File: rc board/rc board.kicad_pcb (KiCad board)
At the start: 2 copper layers, 95 parts, among them J1 Bypass, J10 3S, J11 4S, J12 5S, J13 6S, J14 Mot_0, J15 Mot_1, J16 Mot_3, J17 Mot_2, J2 Bypass, J3 Bypass, J4 Throttle_in, J5 Throttle_out, J6 CH3_in, J7 CH3_out, J8 Steering_in, J9 Steering_out, U1 DRV10983, U2 DRV10983, U3 DRV10983, U4 DRV10983

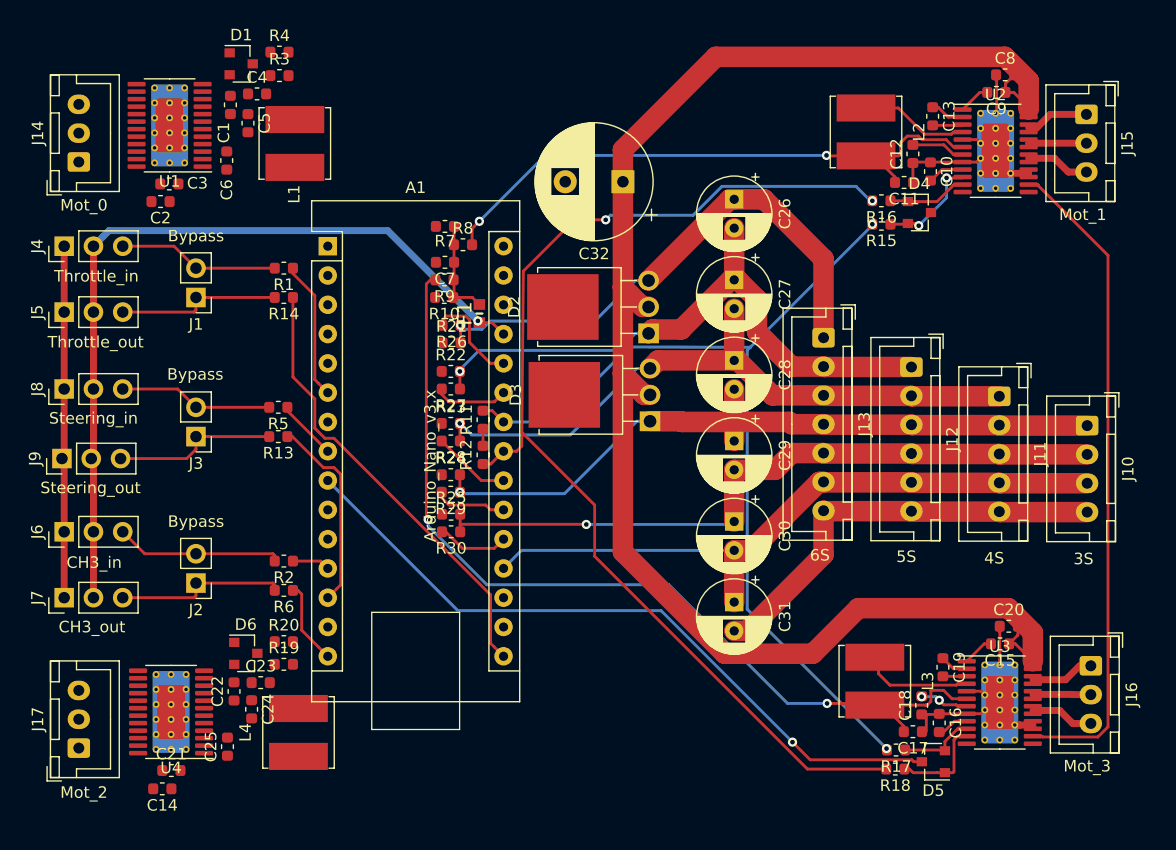
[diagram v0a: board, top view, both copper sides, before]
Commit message: Finished routing all the signals, except for some GNDs that probably need filling.
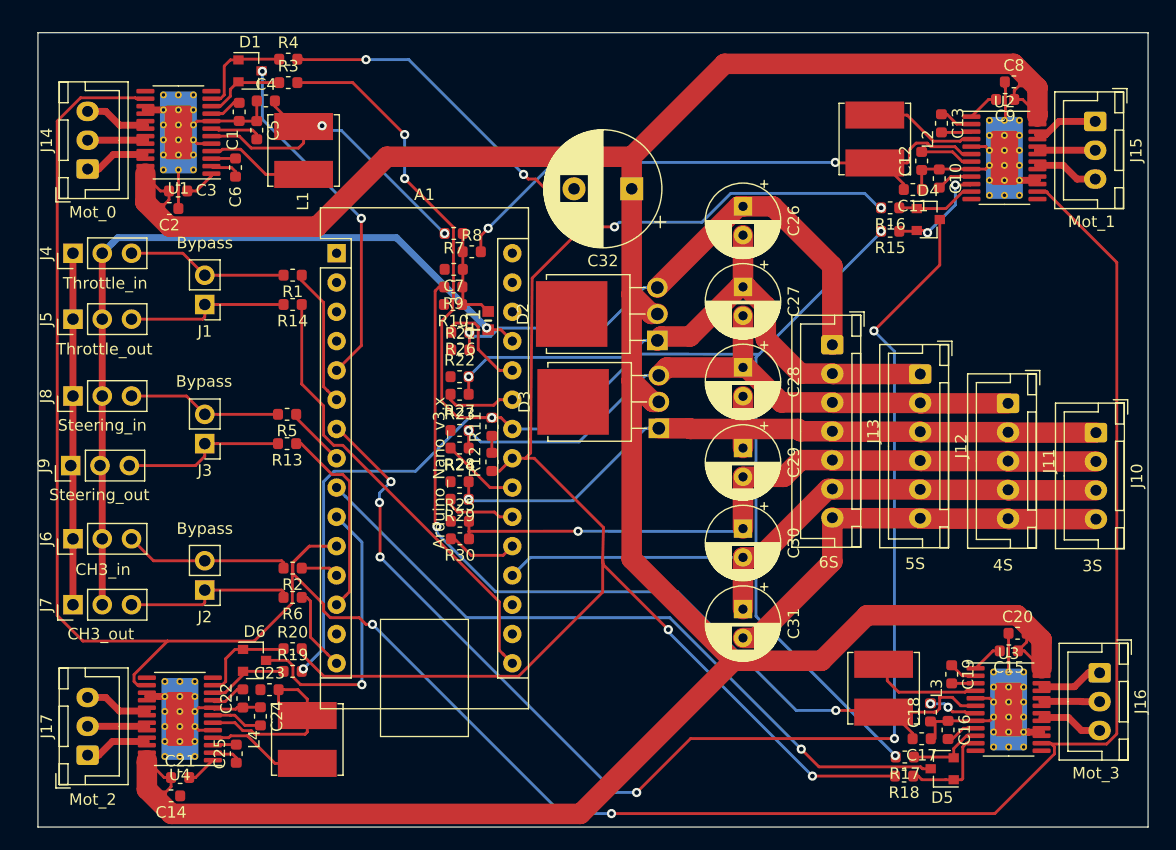
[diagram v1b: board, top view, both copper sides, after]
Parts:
- moved A1 0.98 mm to (40.3, 34.3)
- moved C1 0.98 mm to (31.9, 22.0)
- moved C10 0.98 mm to (92.6, 27.8)
- moved C11 0.98 mm to (90.3, 28.7)
- moved C12 0.98 mm to (91.1, 26.3)
- moved C13 0.98 mm to (92.8, 23.0)
- moved C14 0.98 mm to (26.0, 81.3)
- moved C15 0.98 mm to (98.6, 68.7)
- moved C16 0.98 mm to (93.3, 75.6)
- moved C17 0.98 mm to (91.1, 76.4)
- moved C18 0.98 mm to (91.8, 74.1)
- moved C19 0.98 mm to (93.7, 70.8)
- moved C2 0.98 mm to (25.8, 30.4)
- moved C20 0.98 mm to (99.4, 67.2)
- moved C21 0.98 mm to (26.8, 79.7)
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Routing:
- net DIR: track 57.3 -> 226.3 mm, vias 0 -> 2
- net +BATT: track 137.9 -> 256.3 mm
- net EN_1: track 0.00 -> 116.7 mm, vias 0 -> 6
- net SCL: track 81.4 -> 156.9 mm, vias 2 -> 6
- net SDA: track 99.3 -> 162.6 mm, vias 2 -> 6
- net EN_0: track 0.00 -> 30.5 mm, vias 0 -> 2
- net +5V_0: track 0.00 -> 29.8 mm, vias 0 -> 2
- net EN_3: track 0.00 -> 25.2 mm, vias 0 -> 1
- net GND: track 96.8 -> 121.3 mm
- net +5V_3: track 0.00 -> 15.6 mm
- net Net-(L4-Pad1): track 0.00 -> 9.25 mm
- net Net-(L1-Pad1): track 0.00 -> 8.97 mm
- net Net-(D1-Pad1): track 0.00 -> 8.76 mm
- net Net-(D6-Pad1): track 0.00 -> 8.60 mm
- net Net-(D1-Pad2): track 0.00 -> 7.13 mm
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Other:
- board outline added: 96.3 x 68.9 mm

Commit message: 0 unconnected items!
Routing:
- net +5V_3: track 15.6 -> 60.9 mm, vias 0 -> 6
- net GND: track 121.3 -> 164.2 mm, vias 0 -> 3
- net +3V3: track 1.47 -> 20.3 mm, vias 0 -> 4
- added copper zone on B.Cu, net GND
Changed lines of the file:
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@@
     (thickness 1.6)
     (drawings 4)
-    (tracks 774)
+    (tracks 842)
     (zones 0)
     (modules 95)
@@
   (gr_line (start 110.6932 84.0232) (end 110.6932 15.1384) (layer Edge.Cuts) (width 0.05))
   (gr_line (start 14.4272 15.1384) (end 14.4272 84.0232) (layer Edge.Cuts) (width 0.05))
+  (via (at 50.2412 42.6212) (size 0.8) (drill 0.4) (layers F.Cu B.Cu) (net 16))
+  (via (at 49.6316 35.7124) (size 0.8) (drill 0.4) (layers F.Cu B.Cu) (net 16))
   (segment (start 54.762501 69.024601) (end 55.5625 69.8246) (width 0.25) (layer F.Cu) (net 1))
   (segment (start 54.437499 64.494597) (end 54.437499 68.699599) (width 0.25) (layer F.Cu) (net 1))
@@
   (segment (start 26.6065 27.461364) (end 26.60599 27.461874) (width 0.25) (layer F.Cu) (net 16))
   (segment (start 26.6065 27.0371) (end 26.6065 27.461364) (width 0.25) (layer F.Cu) (net 16))
+  (segment (start 26.6065 20.5371) (end 26.6065 17.8943) (width 3) (layer B.Cu) (net 16))
+  (segment (start 26.6065 27.0371) (end 26.6065 28.6893) (width 3) (layer B.Cu) (net 16))
+  (segment (start 98.234501 22.743601) (end 98.234501 19.469099) (width 3) (layer B.Cu) (net 16))
+  (segment (start 98.234501 29.667865) (end 98.2472 29.680564) (width 3) (layer B.Cu) (net 16))
+  (segment (start 98.234501 29.243601) (end 98.234501 29.667865) (width 3) (layer B.Cu) (net 16))
+  (segment (start 98.2472 29.680564) (end 98.2472 32.9692) (width 3) (layer B.Cu) (net 16))
+  (segment (start 98.596 70.156836) (end 98.6028 70.150036) (width 3) (layer B.Cu) (net 16))
+  (segment (start 98.596 70.5811) (end 98.596 70.156836) (width 3) (layer B.Cu) (net 16))
+  (segment (start 98.6028 70.150036) (end 98.6028 65.532) (width 3) (layer B.Cu) (net 16))
+  (segment (start 98.596 77.505364) (end 98.6028 77.512164) (width 3) (layer B.Cu) (net 16))
+  (segment (start 98.596 77.0811) (end 98.596 77.505364) (width 3) (layer B.Cu) (net 16))
+  (segment (start 98.6028 77.512164) (end 98.6028 80.01) (width 3) (layer B.Cu) (net 16))
+  (segment (start 26.7335 71.4006) (end 26.7335 68.2879) (width 3) (layer B.Cu) (net 16))
+  (segment (start 26.7335 78.324864) (end 26.7208 78.337564) (width 3) (layer B.Cu) (net 16))
+  (segment (start 26.7335 77.9006) (end 26.7335 78.324864) (width 3) (layer B.Cu) (net 16))
+  (segment (start 26.7208 78.337564) (end 26.7208 80.7212) (width 3) (layer B.Cu) (net 16))
+  (segment (start 26.759 77.9261) (end 26.7335 77.9006) (width 0.25) (layer F.Cu) (net 16))
+  (segment (start 26.759 81.3181) (end 26.759 77.9261) (width 0.25) (layer F.Cu) (net 16))
+  (segment (start 33.7185 73.6346) (end 33.7185 72.1106) (width 0.25) (layer F.Cu) (net 16))
+  (segment (start 49.44049 53.75159) (end 49.7655 54.0766) (width 0.25) (layer F.Cu) (net 16))
+  (segment (start 49.44049 49.95661) (end 49.44049 53.75159) (width 0.25) (layer F.Cu) (net 16))
+  (segment (start 49.7655 49.6316) (end 49.44049 49.95661) (width 0.25) (layer F.Cu) (net 16))
+  (segment (start 50.203 49.6316) (end 49.7655 49.6316) (width 0.25) (layer F.Cu) (net 16))
+  (segment (start 49.791 57.5056) (end 50.2285 57.5056) (width 0.25) (layer F.Cu) (net 16))
+  (segment (start 49.44049 57.15509) (end 49.791 57.5056) (width 0.25) (layer F.Cu) (net 16))
+  (segment (start 49.44049 54.40161) (end 49.44049 57.15509) (width 0.25) (layer F.Cu) (net 16))
+  (segment (start 49.7655 54.0766) (end 49.44049 54.40161) (width 0.25) (layer F.Cu) (net 16))
+  (segment (start 50.203 54.0766) (end 49.7655 54.0766) (width 0.25) (layer F.Cu) (net 16))
+  (segment (start 50.203 49.5934) (end 49.784 49.1744) (width 0.25) (layer F.Cu) (net 16))
+  (via (at 49.784 49.1744) (size 0.8) (drill 0.4) (layers F.Cu B.Cu) (net 16))
+  (segment (start 50.203 49.6316) (end 50.203 49.5934) (width 0.25) (layer F.Cu) (net 16))
+  (segment (start 50.203 42.6594) (end 50.2412 42.6212) (width 0.25) (layer F.Cu) (net 16))
+  (segment (start 50.203 44.9707) (end 50.203 42.6594) (width 0.25) (layer F.Cu) (net 16))
   (segment (start 53.7845 50.1016) (end 53.7845 51.5746) (width 0.25) (layer F.Cu) (net 17))
+  (via (at 57.4548 59.436) (size 0.8) (drill 0.4) (layers F.Cu B.Cu) (net 17))
+  (segment (start 57.4548 65.3923) (end 57.4548 59.436) (width 0.25) (layer F.Cu) (net 17))
+  (segment (start 55.5625 67.2846) (end 57.4548 65.3923) (width 0.25) (layer F.Cu) (net 17))
+  (via (at 57.4548 56.4526) (size 0.8) (drill 0.4) (layers F.Cu B.Cu) (net 17))
+  (segment (start 57.4548 59.436) (end 57.4548 56.4526) (width 0.25) (layer B.Cu) (net 17))
+  (via (at 57.4548 54.1528) (size 0.8) (drill 0.4) (layers F.Cu B.Cu) (net 17))
+  (segment (start 57.4548 56.4526) (end 57.4548 54.1528) (width 0.25) (layer F.Cu) (net 17))
+  (segment (start 56.471601 53.169601) (end 55.022499 53.169601) (width 0.25) (layer B.Cu) (net 17))
+  (segment (start 55.022499 53.169601) (end 53.848 51.995102) (width 0.25) (layer B.Cu) (net 17))
+  (segment (start 57.4548 54.1528) (end 56.471601 53.169601) (width 0.25) (layer B.Cu) (net 17))
+  (via (at 53.7845 51.5746) (size 0.8) (drill 0.4) (layers F.Cu B.Cu) (net 17))
+  (segment (start 53.848 51.6381) (end 53.7845 51.5746) (width 0.25) (layer B.Cu) (net 17))
+  (segment (start 53.848 51.995102) (end 53.848 51.6381) (width 0.25) (layer B.Cu) (net 17))
   (segment (start 54.5845 48.5266) (end 55.5625 49.5046) (width 0.25) (layer F.Cu) (net 18))
   (segment (start 53.7845 48.5266) (end 54.5845 48.5266) (width 0.25) (layer F.Cu) (net 18))
@@
   (segment (start 32.925486 75.66058) (end 33.237016 75.97211) (width 0.25) (layer F.Cu) (net 29))
   (segment (start 29.596 74.9756) (end 31.50439 74.9756) (width 0.25) (layer F.Cu) (net 29))
+  (segment (start 37.7825 74.3536) (end 40.9116 74.3536) (width 0.25) (layer F.Cu) (net 29))
+  (via (at 41.7576 72.399601) (size 0.8) (drill 0.4) (layers F.Cu B.Cu) (net 29))
+  (segment (start 38.311499 72.399601) (end 41.7576 72.399601) (width 0.25) (layer F.Cu) (net 29))
+  (segment (start 37.7825 72.9286) (end 38.311499 72.399601) (width 0.25) (layer F.Cu) (net 29))
+  (via (at 41.7946 64.3636) (size 0.8) (drill 0.4) (layers F.Cu B.Cu) (net 29))
+  (segment (start 41.7576 64.4006) (end 41.7946 64.3636) (width 0.25) (layer B.Cu) (net 29))
+  (segment (start 41.7576 72.399601) (end 41.7576 64.4006) (width 0.25) (layer B.Cu) (net 29))
+  (segment (start 41.7946 64.3636) (end 45.5168 60.6414) (width 0.25) (layer F.Cu) (net 29))
+  (via (at 45.385798 56.468202) (size 0.8) (drill 0.4) (layers F.Cu B.Cu) (net 29))
+  (segment (start 45.5168 56.599204) (end 45.385798 56.468202) (width 0.25) (layer F.Cu) (net 29))
+  (segment (start 45.5168 60.6414) (end 45.5168 56.599204) (width 0.25) (layer F.Cu) (net 29))
+  (via (at 46.02377 53.894601) (size 0.8) (drill 0.4) (layers F.Cu B.Cu) (net 29))
+  (segment (start 46.02377 55.83023) (end 46.02377 53.894601) (width 0.25) (layer B.Cu) (net 29))
+  (segment (start 45.385798 56.468202) (end 46.02377 55.83023) (width 0.25) (layer B.Cu) (net 29))
+  (via (at 48.006 38.7604) (size 0.8) (drill 0.4) (layers F.Cu B.Cu) (net 29))
+  (segment (start 46.02377 40.74263) (end 48.006 38.7604) (width 0.25) (layer F.Cu) (net 29))
+  (segment (start 46.02377 53.894601) (end 46.02377 40.74263) (width 0.25) (layer F.Cu) (net 29))
+  (via (at 49.6315 38.7096) (size 0.8) (drill 0.4) (layers F.Cu B.Cu) (net 29))
+  (segment (start 49.5807 38.7604) (end 49.6315 38.7096) (width 0.25) (layer B.Cu) (net 29))
+  (segment (start 48.006 38.7604) (end 49.5807 38.7604) (width 0.25) (layer B.Cu) (net 29))
   (segment (start 33.04149 23.58709) (end 33.401 23.9466) (width 0.25) (layer F.Cu) (net 30))
   (segment (start 33.401 23.9466) (end 33.401 24.3841) (width 0.25) (layer F.Cu) (net 30))
@@
   (segment (start 34.9825 78.5036) (end 32.58949 76.11059) (width 0.25) (layer F.Cu) (net 94))
   (segment (start 37.7825 78.5036) (end 34.9825 78.5036) (width 0.25) (layer F.Cu) (net 94))
+  (zone (net 16) (net_name GND) (layer B.Cu) (hatch edge 0.508)
+    (connect_pads (clearance 0.508))
+    (min_thickness 0.254)
+    (fill yes (arc_segments 32) (thermal_gap 0.508) (thermal_bridge_width 0.508))
+    (polygon
+      (pts
+        (xy 110.6932 15.3924) (xy 110.6424 83.9724) (xy 14.478 84.0232) (xy 14.5288 15.2908)
+      )
+    )
+  )
 )

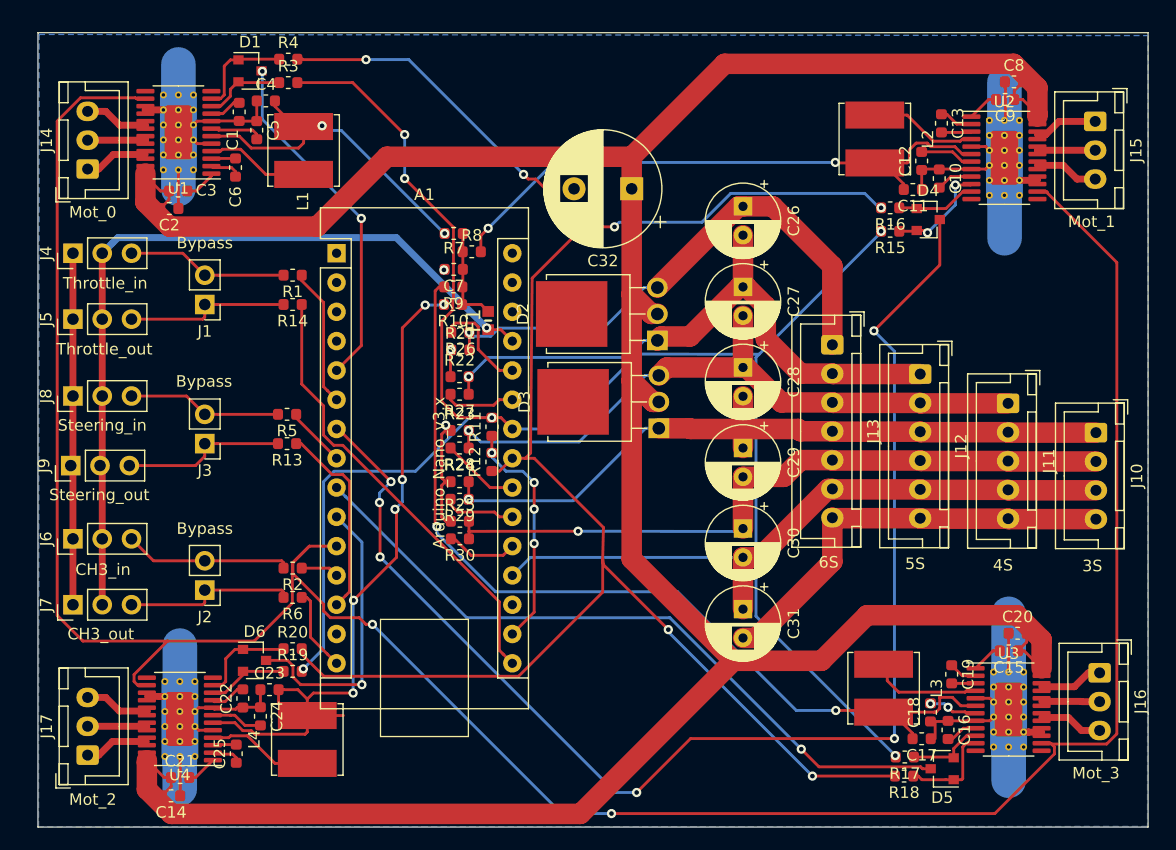
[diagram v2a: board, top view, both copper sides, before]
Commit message: Added fill for GND and +Vbatt as well as a text for the project name and date.
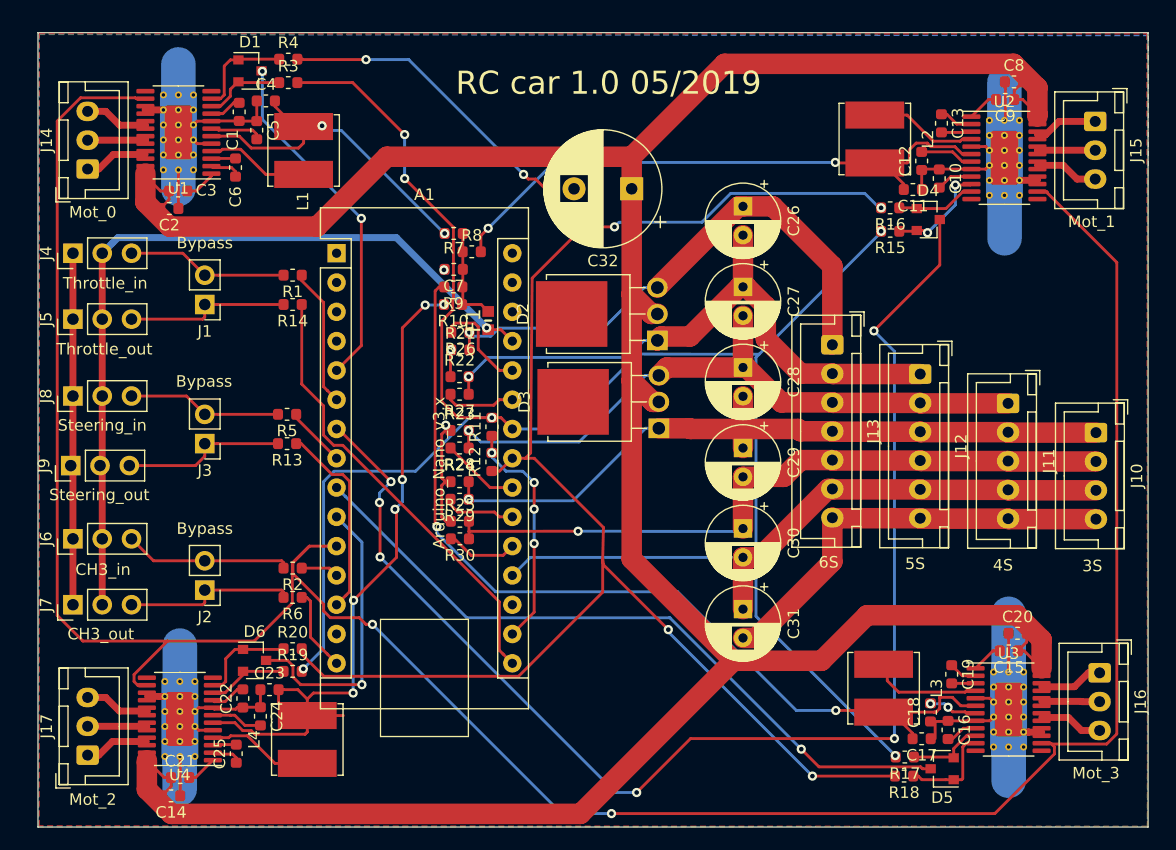
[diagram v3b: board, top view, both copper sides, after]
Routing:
- added copper zone on F.Cu, net +BATT
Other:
- board text added: "RC car 1.0 05/2019"
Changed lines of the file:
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@@
   (general
     (thickness 1.6)
-    (drawings 4)
+    (drawings 5)
     (tracks 842)
     (zones 0)
@@
     )
   )
+  (gr_text "RC car 1.0 05/2019" (at 63.9064 19.5072) (layer F.SilkS)
+    (effects (font (size 2 2) (thickness 0.15)))
+  )
   (gr_line (start 14.4272 15.1384) (end 110.6932 15.1384) (layer Edge.Cuts) (width 0.05))
   (gr_line (start 110.6932 84.0232) (end 14.4272 84.0232) (layer Edge.Cuts) (width 0.05))
@@
       )
     )
+  )
+  (zone (net 22) (net_name +BATT) (layer F.Cu) (hatch edge 0.508)
+    (connect_pads (clearance 0.508))
+    (min_thickness 0.254)
+    (fill yes (arc_segments 32) (thermal_gap 0.508) (thermal_bridge_width 0.508))
+    (polygon
+      (pts
+        (xy 110.6424 83.9724) (xy 14.5288 83.9216) (xy 14.5288 15.24) (xy 110.5916 15.24)
+      )
+    )
